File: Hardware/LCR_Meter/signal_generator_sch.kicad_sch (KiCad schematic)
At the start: 9 parts

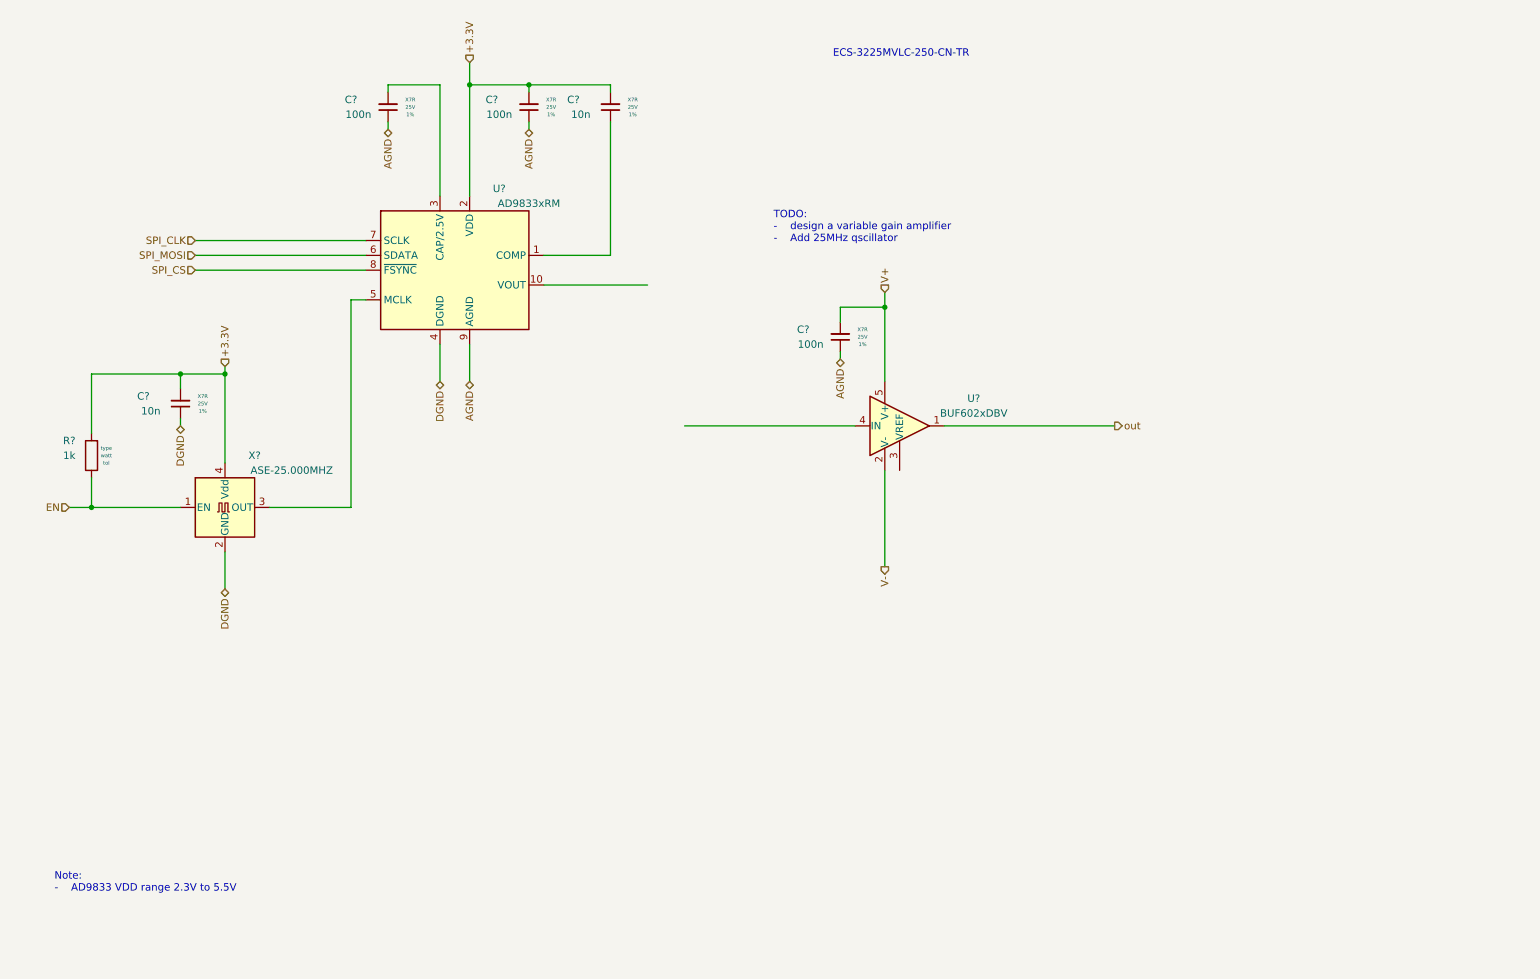
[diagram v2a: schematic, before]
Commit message: work on signal generator
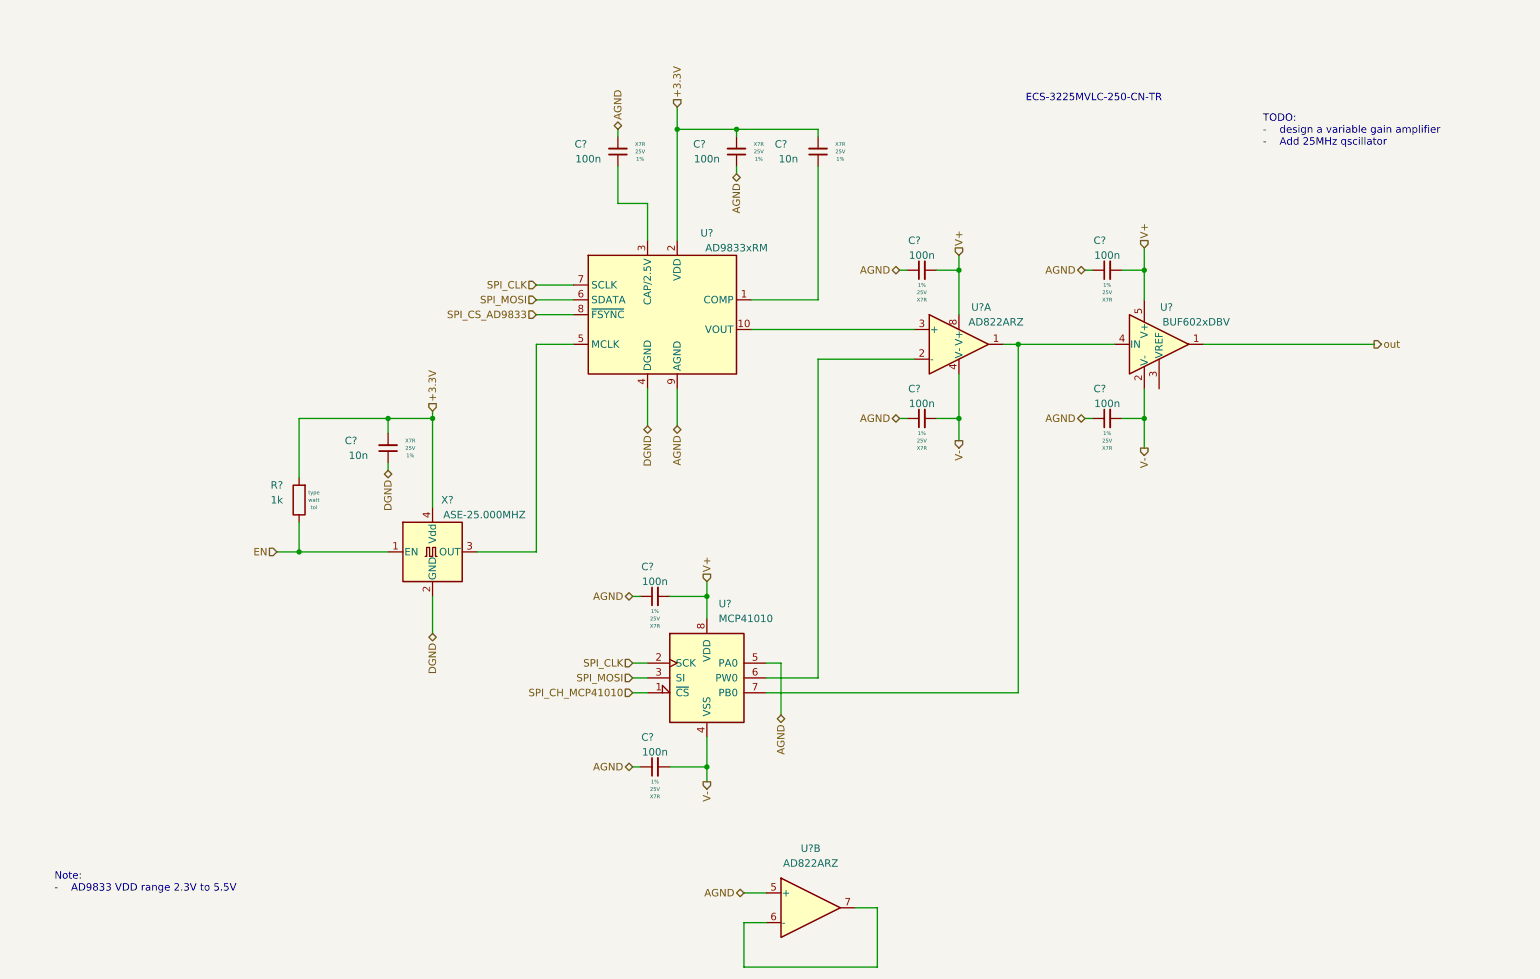
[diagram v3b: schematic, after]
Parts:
- removed C?: 100n, Capacitor_SMD:C_0805_2012Metric_Pad1.18x1.45mm_HandSolder, symbol 010_SMD_Capacitors:C_0805_hs
- added C? (x6): 100n, Capacitor_SMD:C_0805_2012Metric_Pad1.18x1.45mm_HandSolder, symbol 010_SMD_Capacitors:C_0805_hs
- added U? (x2): AD822ARZ, Package_SO:SOIC-8_3.9x4.9mm_P1.27mm, symbol 200_OPAMP:AD822ARZ
- added U?: MCP41010, symbol Potentiometer_Digital:MCP41010
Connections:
- net AGND: now also C?.2, C?.1, C?.1, C?.1, C?.1, C?.1, C?.1, U?.5 (+), U?.5 (PA0); no longer C?.1
- net SPI_CLK: now also U?.2 (SCK)
- net SPI_MOSI: now also U?.3 (SI)
- net V+: now also C?.2, C?.2, C?.2, U?.8 (V+), U?.8 (VDD)
- net V-: now also C?.2, C?.2, C?.2, U?.4 (V-), U?.4 (VSS)
- net at U?.4 (IN): now also U?.1, U?.7 (PB0)
- net at U?.10 (VOUT): now also U?.3 (+)
- net at U?.3 (CAP/2.5V): now also C?.1; no longer C?.2
- net SPI_CS renamed SPI_CS_AD9833
- new net: U?.2 (-), U?.6 (PW0)
- new net: U?.6 (-), U?.7
- new net SPI_CH_MCP41010: U?.1 (~{CS})
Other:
- moved on the sheet: C?, R?, U?, X?

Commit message: work on signal generator
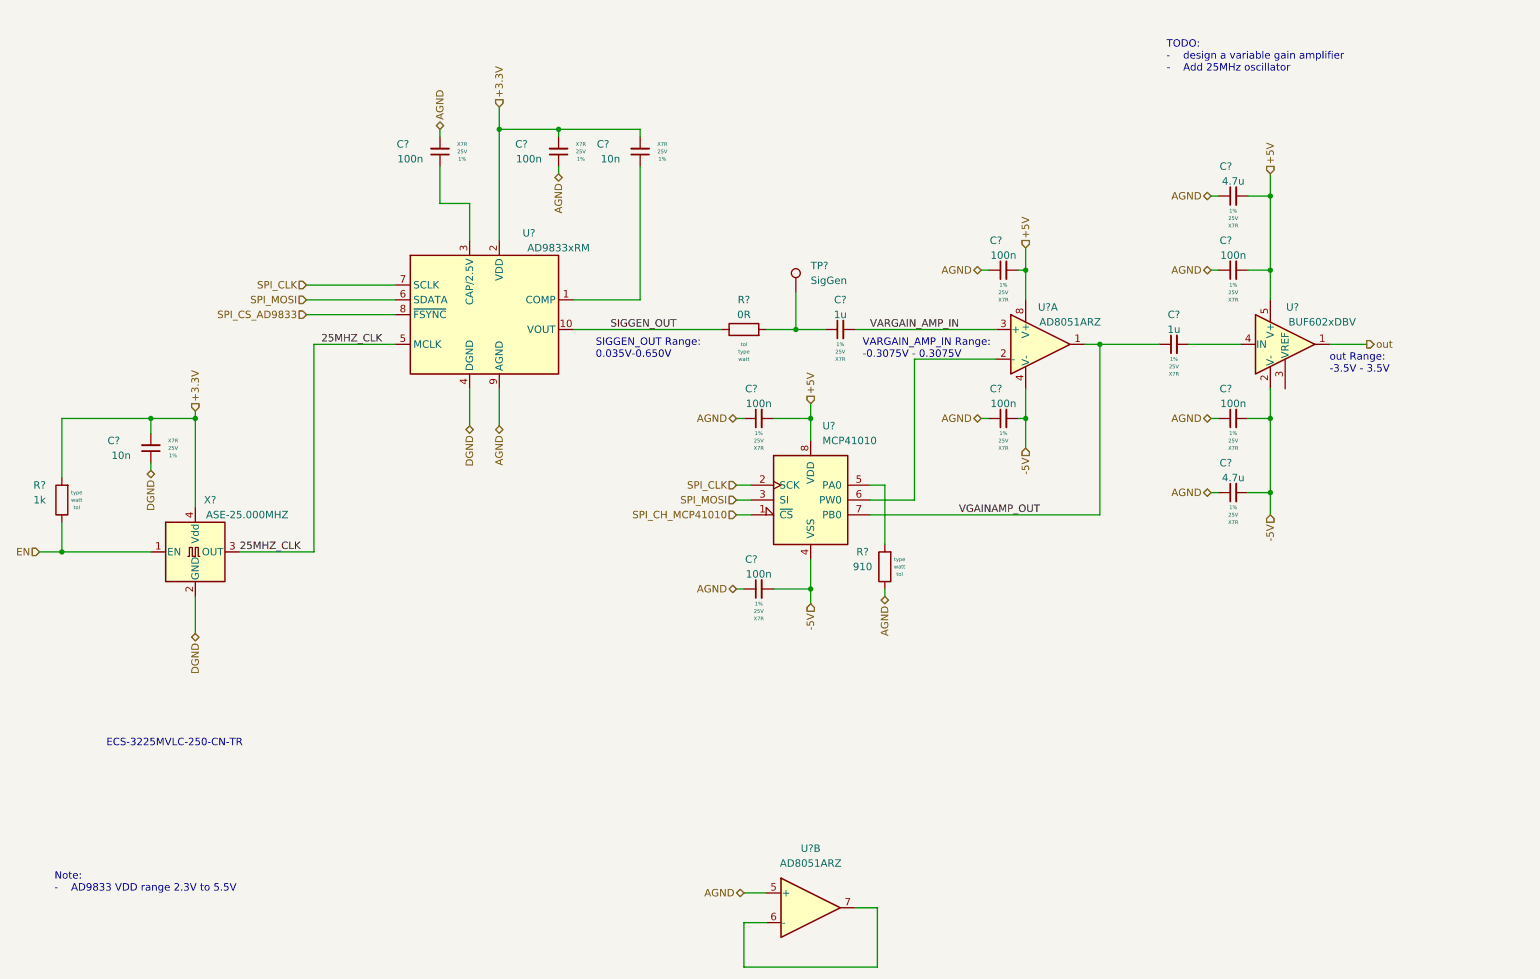
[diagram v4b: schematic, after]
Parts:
- removed C?: 10n, Capacitor_SMD:C_0805_2012Metric_Pad1.18x1.45mm_HandSolder, symbol 010_SMD_Capacitors:C_0805_hs
- removed U? (x2): AD822ARZ, Package_SO:SOIC-8_3.9x4.9mm_P1.27mm, symbol 200_OPAMP:AD822ARZ
- added C? (x2): 4.7u, Capacitor_SMD:C_0805_2012Metric_Pad1.18x1.45mm_HandSolder, symbol 010_SMD_Capacitors:C_0805_hs
- added C?: 10n, Capacitor_SMD:C_0805_2012Metric_Pad1.18x1.45mm_HandSolder, symbol 010_SMD_Capacitors:C_0805_hs
- added C? (x2): 1u, Capacitor_SMD:C_0805_2012Metric_Pad1.18x1.45mm_HandSolder, symbol 010_SMD_Capacitors:C_0805_hs
- added R?: 0R, Resistor_SMD:R_1206_3216Metric, symbol 000_SMD_Resitors:R_1206
- added R?: 910, Resistor_SMD:R_1206_3216Metric, symbol 000_SMD_Resitors:R_1206
- added TP?: SigGen, symbol Connector:TestPoint
- added U? (x2): AD8051ARZ, Package_SO:SOIC-8_3.9x4.9mm_P1.27mm, symbol 200_OPAMP:AD8051ARZ
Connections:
- net +3.3V: now also C?.2
- net AGND: now also C?.1, C?.1, R?.1, U?.5 (+); no longer U?.5 (PA0)
- net at U?.4 (IN): now also C?.2; no longer U?.7 (PB0)
- net at U?.6 (PW0): now also U?.2 (-)
- net SIGGEN_OUT: now reaches U?.10 (VOUT)
- net SIGGEN_OUT: now also R?.1
- net at U?.1 (COMP): now also C?.1
- net 25MHZ_CLK: now reaches U?.5 (MCLK), X?.3 (OUT)
- net V+ renamed +5V
- net +5V: now also C?.2, U?.8 (V+)
- net V- renamed -5V
- net -5V: now also C?.2, U?.4 (V-)
- new net: C?.1, R?.2, TP?.1
- new net: R?.2, U?.5 (PA0)
- new net: U?.6 (-), U?.7
- new net VARGAIN_AMP_IN: C?.2, U?.3 (+)
- new net VGAINAMP_OUT: C?.1, U?.1, U?.7 (PB0)
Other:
- note added: "SIGGEN_OUT Range: 0.035V-0.650V"
- note added: "TODO: - design a variable gain amplifier - Add 25MHz oscillator"
- note added: "VARGAIN_AMP_IN Range: -0.3075V - 0.3075V"
- note added: "out Range: -3.5V - 3.5V"
- note removed: "TODO: - design a variable gain amplifier - Add 25MHz qscillator"
- moved on the sheet: C?, R?, U?, X?
